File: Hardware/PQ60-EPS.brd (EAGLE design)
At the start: 42 x 42 mm, 77 parts, among them IC1 LTC4413, IC3 MKL05Z32VFM4, J1 FTS-105-01-L-D, X1-BOT FX8C-60S-SV, X1-TOP FX8C-60P-SV

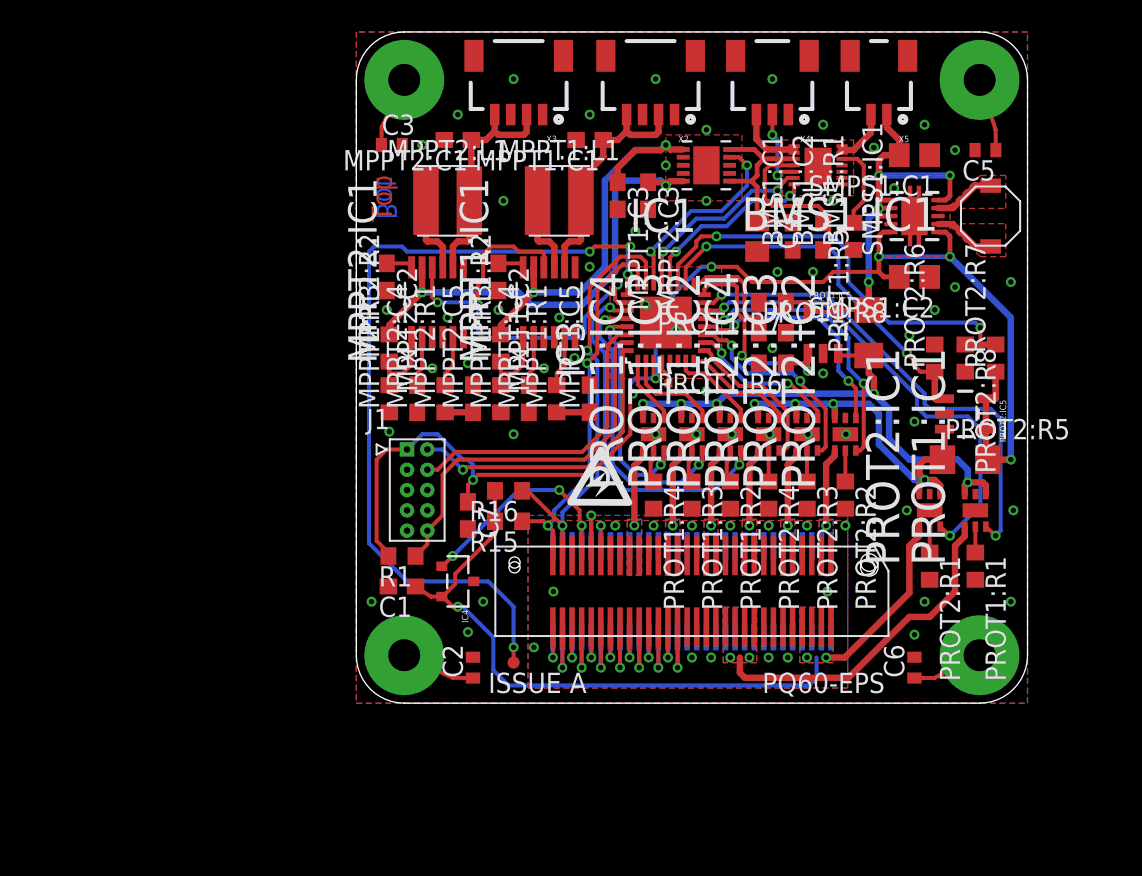
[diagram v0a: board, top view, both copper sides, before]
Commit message: Broken out some modules. Swapping SMPS.
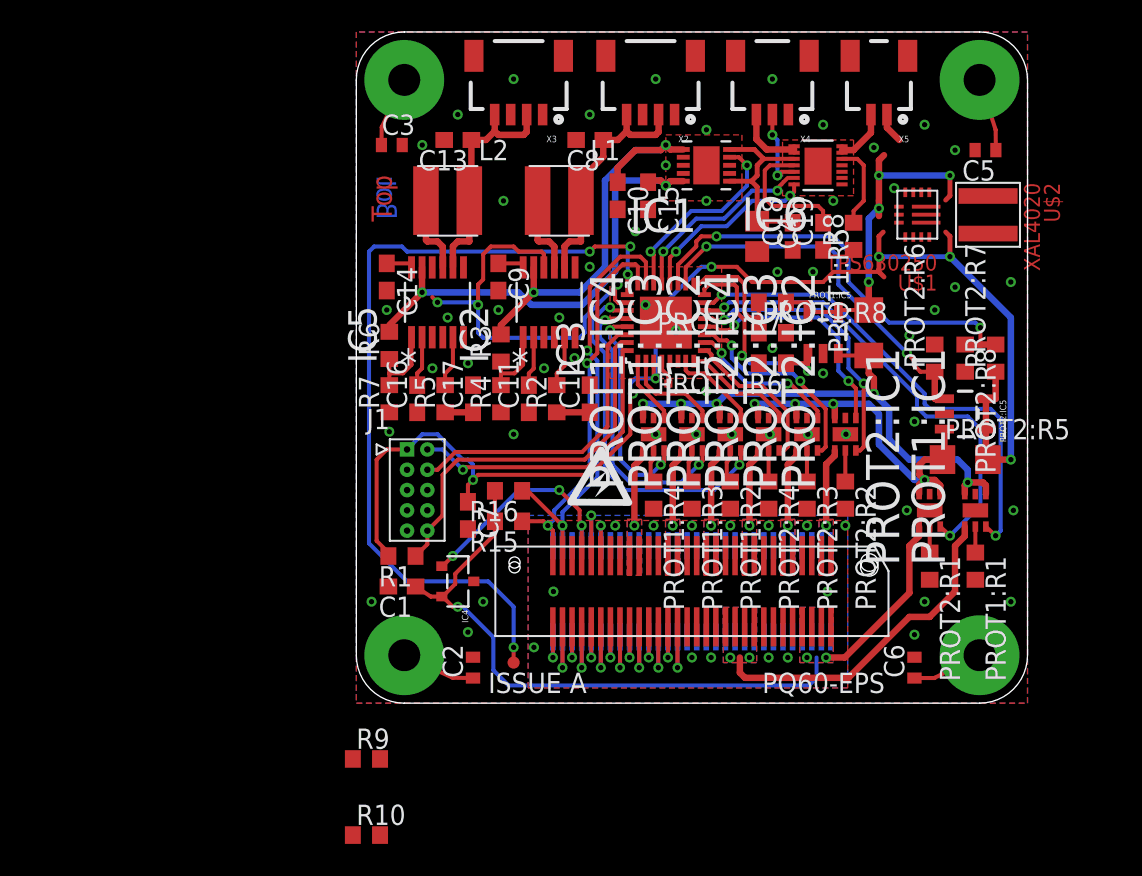
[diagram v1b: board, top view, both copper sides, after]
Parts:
- removed MPPT2:R2: 1M33, rcl:R0603
- removed SMPS1:C1, SMPS1:C2: 10uF, rcl:C0805
- removed SMPS1:IC1: TPS63001, texas:DRC-S-PVSON-N10
- removed SMPS1:L1: 2.2uH, SparkFun-Passives:VLF4012A
- added R10, R9: 2k, rcl:R0603
- added R6: 1M33, rcl:R0603
- added U$1: TPS630250, ears-pq:VQFN14
- added U$2: XAL4020, ears-pq:XAL4020
- renumbered BMS1:C1 to C18, BMS1:C2 to C19, BMS1:IC1 to IC6, BMS1:R1 to R8, MPPT1:C1 to C8, MPPT1:C2 to C9, MPPT1:C3 to C10, MPPT1:C4 to C11, MPPT1:C5 to C12, MPPT1:IC1 to IC2, MPPT1:L1 to L1, MPPT1:R1 to R2, MPPT1:R2 to R3, MPPT1:R3 to R4, MPPT2:C1 to C13, MPPT2:C2 to C14, MPPT2:C3 to C15, MPPT2:C4 to C16, MPPT2:C5 to C17, MPPT2:IC1 to IC5, MPPT2:L1 to L2, MPPT2:R1 to R5, MPPT2:R3 to R7
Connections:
- net BMS1:BATT_PROG renamed BATT_PROG
- net BMS1:VL renamed VL
- net MPPT1:!SHDN! renamed !SHDN1!
- net MPPT1:AUX renamed AUX1
- net MPPT1:FB renamed FB1
- net MPPT1:LDO renamed LDO1
- net MPPT1:MPPC renamed MPPC1
- net MPPT1:SW renamed SW1
- net MPPT1:THM renamed THM1
- net MPPT2:!SHDN! renamed !SHDN2!
- net MPPT2:AUX renamed AUX2
- net MPPT2:LDO renamed LDO2
- net MPPT2:MPPC renamed MPPC2
- net MPPT2:SW renamed SW2
- net MPPT2:THM renamed THM2
- removed net MPPT2:FB: IC5.1, MPPT2:R2.1, R7.2
- removed net SMPS1:N$1: SMPS1:IC1.4, SMPS1:L1.P$1
- removed net SMPS1:N$2: SMPS1:IC1.2, SMPS1:L1.P$2
- new net FB2: IC5.1, R6.1, R7.2
- new net N$6: U$1.P$3, U$2.P$1
- new net N$7: U$1.P$1, U$2.P$2
- new net N$9: R10.2, R9.1, U$1.P$11
- new net PGOOD: IC5.10
- net +3V3_UNPRO: now also R9.2; no longer SMPS1:C2.2, SMPS1:IC1.1, SMPS1:IC1.10
- net GND: now also R10.1, U$1.P$10, U$1.P$2, U$1.P$9; no longer SMPS1:C1.1, SMPS1:C2.1, SMPS1:IC1.3, SMPS1:IC1.9, SMPS1:IC1.TH, SMPS1:IC1.TH@1, SMPS1:IC1.TH@2
- net MPPT_PGD: no longer IC5.10
- net S_ARRAY_2: now also R6.2; no longer MPPT2:R2.2
- net VSYS_SW: now also U$1.P$4, U$1.P$5, U$1.P$6, U$1.P$7, U$1.P$8; no longer SMPS1:C1.2, SMPS1:IC1.5, SMPS1:IC1.6, SMPS1:IC1.7, SMPS1:IC1.8
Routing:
- net MPPT2:FB: track 4.81 -> 0.00 mm
- net FB2: track 0.00 -> 4.81 mm
- net VSYS_SW: track 29.1 -> 24.5 mm
- net SMPS1:N$2: track 3.87 -> 0.00 mm
- net SMPS1:N$1: track 3.87 -> 0.00 mm
- net +3V3_UNPRO: track 86.4 -> 84.5 mm
- net MPPT_PGD: track 27.7 -> 25.8 mm
- net THM2: track 1.75 -> 0.00 mm
- net MPPT2:THM: track 0.00 -> 1.75 mm
- removed copper zone on layer 1, net SMPS1:N$1
- removed copper zone on layer 1, net SMPS1:N$2

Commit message: pre deleting prot modules
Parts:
- removed R10, R9: 2k, rcl:R0603
- added C20, C21: 10uF, rcl:C0603
- added U$3, U$5, U$6: INA3221, ears-pq:VQFN16
- added U$4, U$7, U$8, U$9: TPS2052B, ears-pq:8SON
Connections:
- net N$6 renamed L1
- net N$7 renamed L2
- new net 3V3_PRO: PROT2:IC1.1, U$6.P$14
- new net N$10: U$5.P$15, U$8.P$7
- new net N$11: U$5.P$2, U$9.P$6
- new net N$12: U$6.P$12, U$9.P$7
- new net N$13: U$6.P$15, U$7.P$7
- new net N$6: U$3.P$12, U$4.P$6
- new net N$7: U$3.P$15, U$4.P$7
- new net N$8: U$3.P$2, U$7.P$6
- net +3V3_SW[1]: now also U$3.P$11
- net +3V3_SW[2]: now also U$3.P$14
- net +3V3_SW[3]: now also U$3.P$1
- net +3V3_UNPRO: now also C21.1, U$1.P$11, U$1.P$12, U$1.P$13, U$1.P$14, U$4.P$2, U$7.P$2; no longer R9.2
- net GND: now also C20.2, C21.2, U$3.P$3, U$3.P$5, U$4.P$1, U$5.P$3, U$6.P$3, U$7.P$1, U$8.P$1, U$9.P$1; no longer R10.1
- net I2C_SCL: now also U$3.P$6, U$5.P$5, U$5.P$6, U$6.P$6
- net I2C_SDA: now also U$3.P$7, U$5.P$7, U$6.P$5, U$6.P$7
- net N$9: now also U$5.P$12, U$8.P$6; no longer R10.2, R9.1, U$1.P$11
- net PRO1: no longer PROT2:IC1.1
- net VBAT: now also U$6.P$11
- net VBAT_SW[1]: now also U$5.P$11
- net VBAT_SW[1]_EN: now also U$8.P$3
- net VBAT_SW[2]: now also U$5.P$14
- net VBAT_SW[2]_EN: now also U$8.P$4
- net VBAT_SW[3]: now also U$5.P$1
- net VBAT_SW[3]_EN: now also U$9.P$3
- net VSYS_SW: now also C20.1, U$3.P$4, U$5.P$4, U$6.P$4, U$8.P$2, U$9.P$2, U$9.P$4
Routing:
- net PRO1: track 49.5 -> 38.2 mm, vias 3 -> 2
- net VSYS_SW: track 24.5 -> 26.0 mm, vias 4 -> 2
- net +3V3_UNPRO: track 84.5 -> 86.0 mm, vias 7 -> 6
- added copper zone on layer 1, net L1
- added copper zone on layer 1, net L2

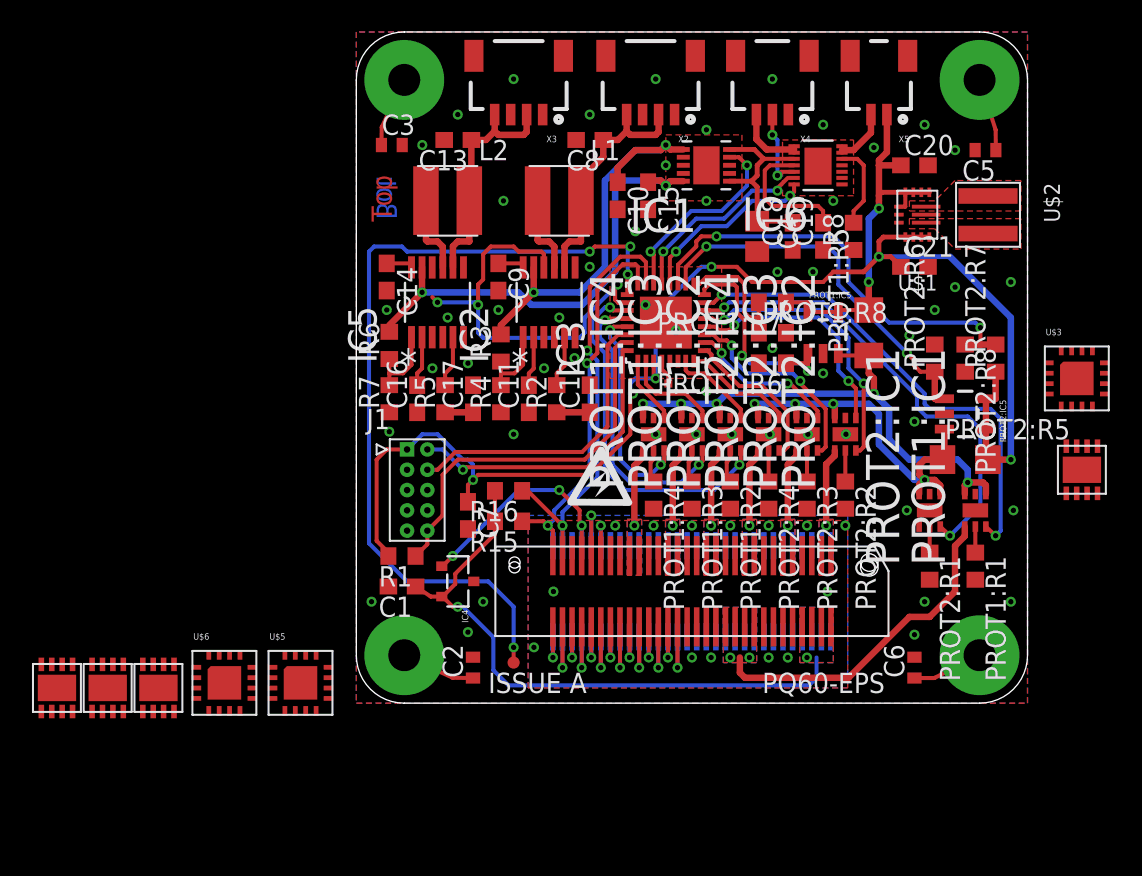
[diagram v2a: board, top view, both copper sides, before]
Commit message: routed most of the power
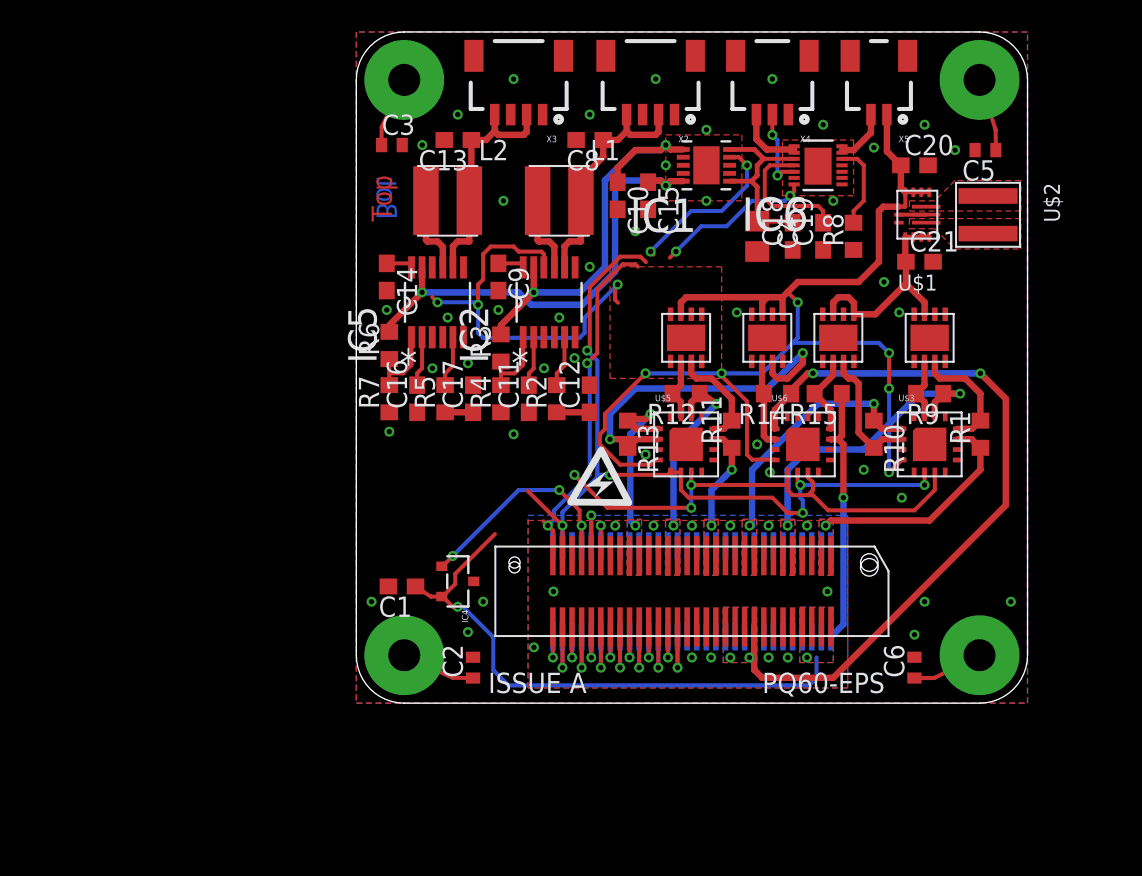
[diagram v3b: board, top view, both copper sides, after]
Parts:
- removed C7: 100nF, rcl:C0603
- removed IC3: MKL05Z32VFM4, general:QFN50P500X500X100-33N
- removed J1: FTS-105-01-L-D, general:SAMTEC_FTS-105-01-L-D
- removed PROT1:IC1, PROT1:IC2, PROT1:IC3, PROT1:IC4, PROT2:IC1, PROT2:IC2, PROT2:IC3, PROT2:IC4: TPS2553DRVT, general:SON65P200X200X80-7N
- removed PROT1:IC5, PROT2:IC5: (no value), SparkFun-AnalogIC:SOT23-5
- removed PROT1:R1, PROT2:R1: 27k, rcl:R0603
- removed PROT1:R2, PROT1:R3, PROT1:R4, PROT2:R2, PROT2:R3, PROT2:R4: 52k, rcl:R0603
- removed PROT1:R5, PROT2:R5: 0R025, rcl:R1206
- removed PROT1:R6, PROT2:R6: 10k 1%, rcl:R0603
- removed PROT1:R7, PROT2:R7: 820k 1%, rcl:R0603
- removed PROT1:R8, PROT2:R8: 200k 1%, rcl:R0603
- removed R16: DNP, rcl:R0603
- removed TP1: TEST-POINT2, SparkFun-Passives:PAD.02X.02
- removed TP2: TEST-POINT3, SparkFun-Passives:PAD.03X.03
- added R10, R11, R12, R13, R14, R9: 1M33, rcl:R0603
- R1: value 10k -> 1M33
- R15: value DNP -> 1M33
- moved U$9 49.6 mm to (25.7, 22.9)
- moved U$7 47.9 mm to (30.2, 22.9)
- moved U$8 42.3 mm to (20.6, 22.9)
- moved U$6 39.2 mm to (27.9, 16.2)
- moved R1 37.0 mm to (39.1, 16.8), turned to 90 degrees
- moved U$5 28.4 mm to (20.6, 16.2)
- moved R15 21.5 mm to (29.5, 19.4)
- moved U$4 12.6 mm to (35.9, 22.9)
- moved U$3 10.1 mm to (35.9, 16.2)
- moved C21 0.45 mm to (35.2, 27.6)
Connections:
- removed net +3V3_I_SEN: IC3.18, PROT2:IC5.1, PROT2:R6.1
- removed net +3V3_SW[0]_!FAULT!: IC3.14, PROT2:IC1.3
- removed net +3V3_SW[1]_!FAULT!: IC3.13, PROT2:IC2.3
- removed net +3V3_SW[1]_EN: IC3.12, PROT2:IC2.4
- removed net +3V3_SW[2]_!FAULT!: IC3.11, PROT2:IC3.3
- removed net +3V3_SW[2]_EN: IC3.10, PROT2:IC3.4
- removed net +3V3_SW[3]_!FAULT!: IC3.9, PROT2:IC4.3
- removed net +3V3_SW[3]_EN: IC3.8, PROT2:IC4.4
- removed net +3V3_V_SEN: IC3.19, PROT2:R7.2, PROT2:R8.1
- removed net I2C_INT: IC3.25, TP2.P$1
- removed net N$5: IC3.4, TP1.P$1
- removed net PRO1: C1.1, IC4.2, R15.2, R16.2, X1-BOT.57, X1-BOT.58, X1-BOT.59, X1-BOT.60, X1-TOP.57, X1-TOP.58, X1-TOP.59, X1-TOP.60
- removed net PROT1:IN_SEN: PROT1:IC1.4, PROT1:IC1.6, PROT1:IC2.6, PROT1:IC3.6, PROT1:IC4.6, PROT1:IC5.3, PROT1:R5.1
- removed net PROT1:I_LIM_SW1: PROT1:IC2.2, PROT1:R2.1
- removed net PROT1:I_LIM_SW2: PROT1:IC3.2, PROT1:R3.1
- removed net PROT1:I_LIM_SW3: PROT1:IC4.2, PROT1:R4.1
- removed net PROT1:I_LIM_VCC: PROT1:IC1.2, PROT1:R1.1
- removed net PROT2:IN_SEN: PROT2:IC1.4, PROT2:IC1.6, PROT2:IC2.6, PROT2:IC3.6, PROT2:IC4.6, PROT2:IC5.3, PROT2:R5.1
- removed net PROT2:I_LIM_SW1: PROT2:IC2.2, PROT2:R2.1
- removed net PROT2:I_LIM_SW2: PROT2:IC3.2, PROT2:R3.1
- removed net PROT2:I_LIM_SW3: PROT2:IC4.2, PROT2:R4.1
- removed net PROT2:I_LIM_VCC: PROT2:IC1.2, PROT2:R1.1
- removed net RESET: IC3.31, J1.10, R1.1
- removed net SWD_CLK: IC3.30, J1.4
- removed net SWD_DIO: IC3.32, J1.2
- removed net VBAT_I_SEN: IC3.16, PROT1:IC5.1, PROT1:R6.1
- removed net VBAT_SW[0]_!FAULT!: IC3.15, PROT1:IC1.3
- removed net VBAT_SW[1]_!FAULT!: IC3.27, PROT1:IC2.3
- removed net VBAT_SW[2]_!FAULT!: IC3.28, PROT1:IC3.3
- removed net VBAT_SW[3]_!FAULT!: IC3.29, PROT1:IC4.3
- removed net VBAT_V_SEN: IC3.17, PROT1:R7.2, PROT1:R8.1
- net +3V3_SW[1]: now also R1.1; no longer PROT2:IC2.1
- net +3V3_SW[2]: now also R9.1; no longer PROT2:IC3.1
- net +3V3_SW[3]: now also R10.1; no longer PROT2:IC4.1
- net +3V3_UNPRO: now also U$7.P$4; no longer C7.1, IC3.3, J1.1, PROT2:IC5.4, PROT2:IC5.5, PROT2:R5.2, PROT2:R7.1, R1.2
- net 3V3_PRO: now also C1.1, IC4.2, R15.1, U$6.P$11, X1-BOT.57, X1-BOT.58, X1-BOT.59, X1-BOT.60, X1-TOP.57, X1-TOP.58, X1-TOP.59, X1-TOP.60; no longer PROT2:IC1.1, U$6.P$14
- net BMS_!CHG!: no longer IC3.21
- net BMS_!PGD!: no longer IC3.20
- net GND: no longer C7.2, IC3.33, IC3.5, IC3.6, J1.3, J1.5, J1.7, J1.9, PROT1:IC1.5, PROT1:IC1.7, PROT1:IC2.5, PROT1:IC2.7, PROT1:IC3.5, PROT1:IC3.7, PROT1:IC4.5, PROT1:IC4.7, PROT1:IC5.2, PROT1:R1.2, PROT1:R2.2, PROT1:R3.2, PROT1:R4.2, PROT1:R6.2, PROT1:R8.2, PROT2:IC1.5, PROT2:IC1.7, PROT2:IC2.5, PROT2:IC2.7, PROT2:IC3.5, PROT2:IC3.7, PROT2:IC4.5, PROT2:IC4.7, PROT2:IC5.2, PROT2:R1.2, PROT2:R2.2, PROT2:R3.2, PROT2:R4.2, PROT2:R6.2, PROT2:R8.2
- net I2C_SCL: no longer IC3.23, R16.1
- net I2C_SDA: no longer IC3.24, R15.1
- net IDIODE_STAT: no longer IC3.22
- net MPPT_PGD: no longer IC3.26
- net N$10: now also R12.2
- net N$11: now also R13.2
- net N$12: now also R14.2, U$6.P$2; no longer U$6.P$12
- net N$13: now also R15.2, U$6.P$12; no longer U$6.P$15
- net N$6: now also R1.2
- net N$7: now also R9.2
- net N$8: now also R10.2
- net N$9: now also R11.2
- net VBAT: now also R14.1, U$6.P$1; no longer PROT1:IC1.1, U$6.P$11
- net VBAT_SW[1]: now also R11.1; no longer PROT1:IC2.1
- net VBAT_SW[1]_EN: no longer IC3.7, PROT1:IC2.4
- net VBAT_SW[2]: now also R12.1; no longer PROT1:IC3.1
- net VBAT_SW[2]_EN: no longer IC3.2, PROT1:IC3.4
- net VBAT_SW[3]: now also R13.1; no longer PROT1:IC4.1
- net VBAT_SW[3]_EN: no longer IC3.1, PROT1:IC4.4
- net VSYS_SW: no longer PROT1:IC5.4, PROT1:IC5.5, PROT1:R5.2, PROT1:R7.1
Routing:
- net +3V3_UNPRO: track 86.0 -> 13.9 mm, vias 6 -> 0
- net I2C_INT: track 52.3 -> 0.00 mm, vias 4 -> 0
- net 3V3_PRO: track 0.00 -> 51.8 mm, vias 0 -> 3
- net VSYS_SW: track 26.0 -> 75.1 mm, vias 2 -> 6
- net PRO1: track 38.2 -> 0.00 mm, vias 2 -> 0
- net PROT1:IN_SEN: track 34.3 -> 0.00 mm, vias 5 -> 0
- net VBAT_SW[0]_!FAULT!: track 30.6 -> 0.00 mm, vias 2 -> 0
- net +3V3_SW[0]_!FAULT!: track 29.5 -> 0.00 mm, vias 2 -> 0
- net I2C_SDA: track 25.7 -> 54.5 mm, vias 2 -> 5
- net +3V3_V_SEN: track 27.5 -> 0.00 mm, vias 2 -> 0
- net VBAT: track 21.1 -> 47.1 mm, vias 2 -> 4
- net I2C_SCL: track 28.5 -> 52.7 mm, vias 2 -> 6
- net PROT2:IN_SEN: track 24.0 -> 0.00 mm, vias 4 -> 0
- net +3V3_I_SEN: track 23.9 -> 0.00 mm, vias 2 -> 0
- net RESET: track 23.7 -> 0.00 mm
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- added copper zone on layer 1, net 3V3_PRO
- added copper zone on layer 16, net 3V3_PRO
- removed copper zone on layer 1, net PRO1
- removed copper zone on layer 16, net PRO1
